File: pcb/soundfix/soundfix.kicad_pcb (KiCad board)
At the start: 2 copper layers, 55.2 x 37.2 mm, 42 parts, among them J1 CONN_02X05, J2 CONN_01X02, J3 CONN_01X02, U1 TL074, U2 TDA7050, U3 TDA7050

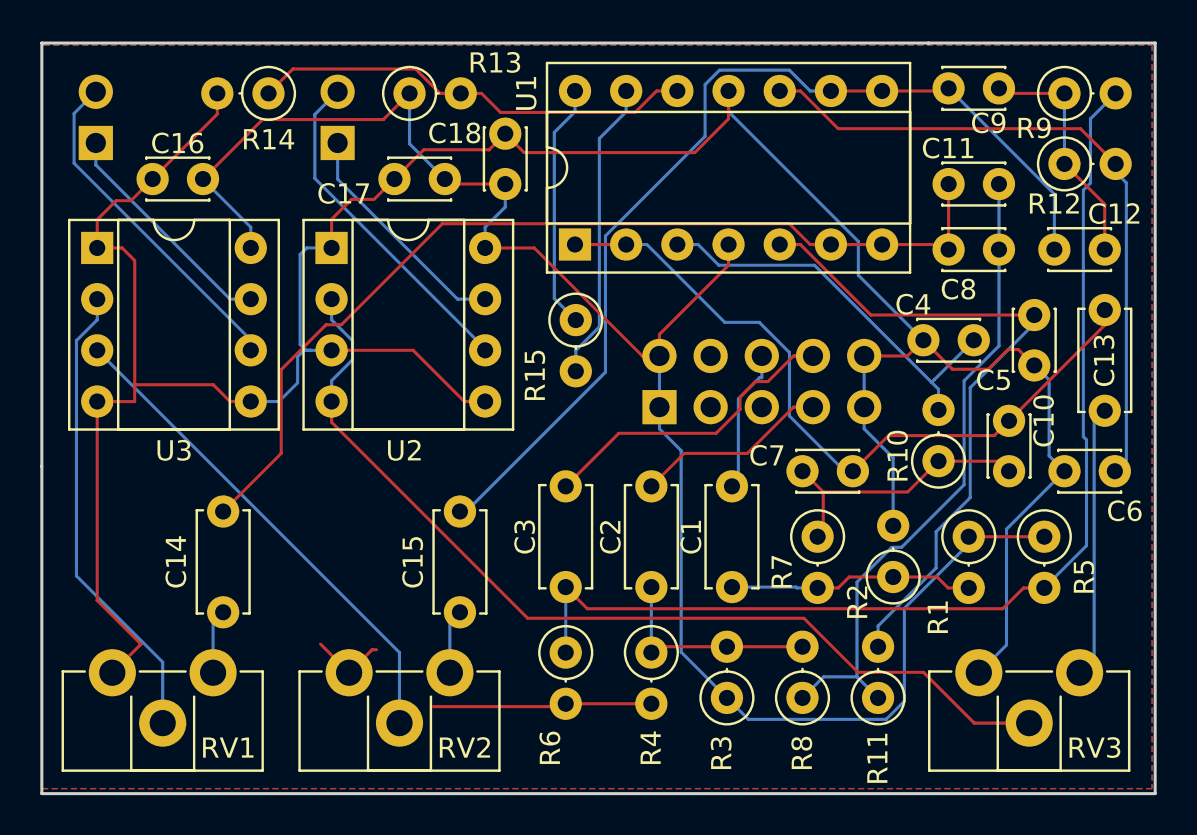
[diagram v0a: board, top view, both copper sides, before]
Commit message: Migrate other PCBs from KiCad 4 to KiCad 8
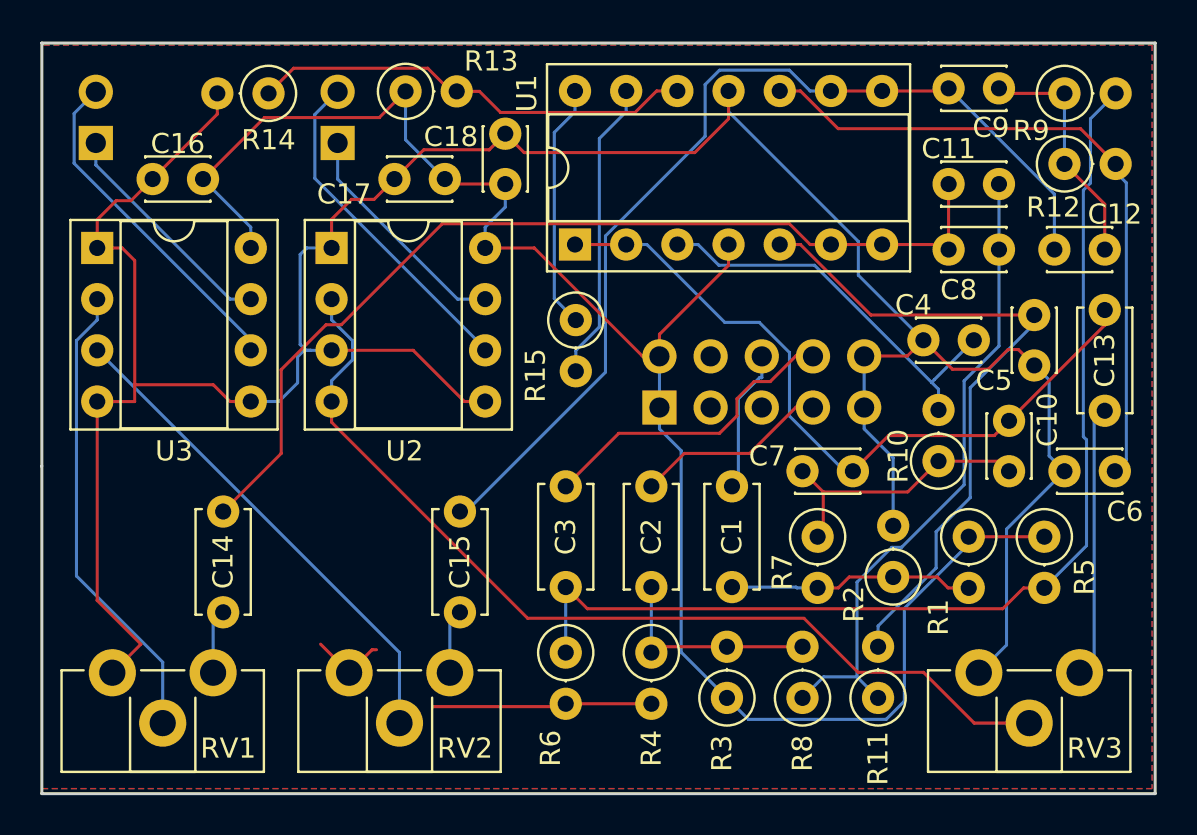
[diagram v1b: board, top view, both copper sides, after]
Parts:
- C1, C13, C14, C15, C2, C3: footprint Capacitors_THT:C_Disc_D5.0mm_W2.5mm_P5.00mm -> Capacitor_THT:C_Disc_D5.0mm_W2.5mm_P5.00mm
- C10, C11, C12, C16, C17, C18, C4, C5, C6, C7, C8, C9: footprint Capacitors_THT:C_Disc_D3.0mm_W2.0mm_P2.50mm -> Capacitor_THT:C_Disc_D3.0mm_W2.0mm_P2.50mm
- J1: value CONN_02X05 -> Conn_02x05_Odd_Even; footprint Pin_Headers:Pin_Header_Straight_2x05_Pitch2.54mm -> Connector_PinSocket_2.54mm:PinSocket_2x05_P2.54mm_Vertical
- J2, J3: value CONN_01X02 -> Conn_01x02; footprint Pin_Headers:Pin_Header_Straight_1x02_Pitch2.54mm -> Connector_PinHeader_2.54mm:PinHeader_1x02_P2.54mm_Vertical
- R1, R10, R11, R12, R13, R14, R15, R2, R3, R4, R5, R6, R7, R8, R9: footprint Resistors_THT:R_Axial_DIN0207_L6.3mm_D2.5mm_P2.54mm_Vertical -> Resistor_THT:R_Axial_DIN0207_L6.3mm_D2.5mm_P2.54mm_Vertical
- RV1, RV2, RV3: footprint Potentiometers:Potentiometer_Trimmer_ACP_CA9h2.5_Vertical_Px2.5mm_Py5.0mm -> Potentiometer_THT:Potentiometer_ACP_CA9-H2,5_Horizontal
- U1: footprint Housings_DIP:DIP-14_W7.62mm_Socket -> Package_DIP:DIP-14_W7.62mm_Socket
- U2, U3: footprint Housings_DIP:DIP-8_W7.62mm_Socket -> Package_DIP:DIP-8_W7.62mm_Socket
- moved R13 0.22 mm to (85.0, 144.4)
- moved J1 0.05 mm to (97.7, 160.1)
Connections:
- J1 pad 3: Net-(J1-Pad3) -> unconnected-(J1-Pin_3-Pad3)
- J1 pad 4: Net-(J1-Pad4) -> unconnected-(J1-Pin_4-Pad4)
- J1 pad 5: Net-(J1-Pad5) -> unconnected-(J1-Pin_5-Pad5)
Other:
- net class Default removed
